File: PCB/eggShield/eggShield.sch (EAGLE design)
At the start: 23 parts, among them U1 V_REG_LDOSMD, U2 V_REG_LDOSMD

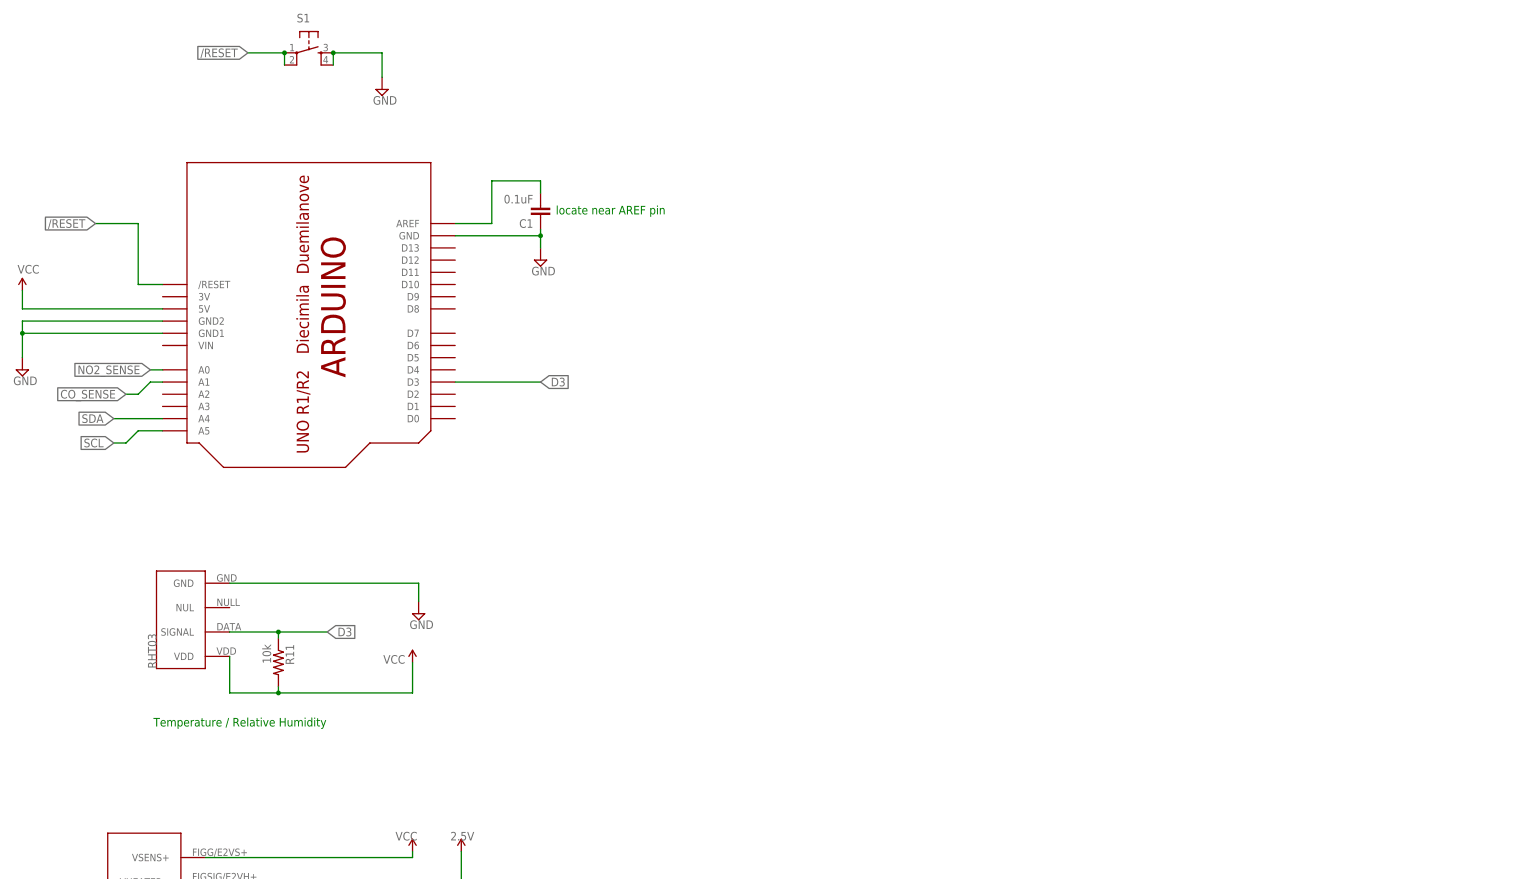
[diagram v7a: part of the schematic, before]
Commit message: added 2:1 I2C Multiplexer
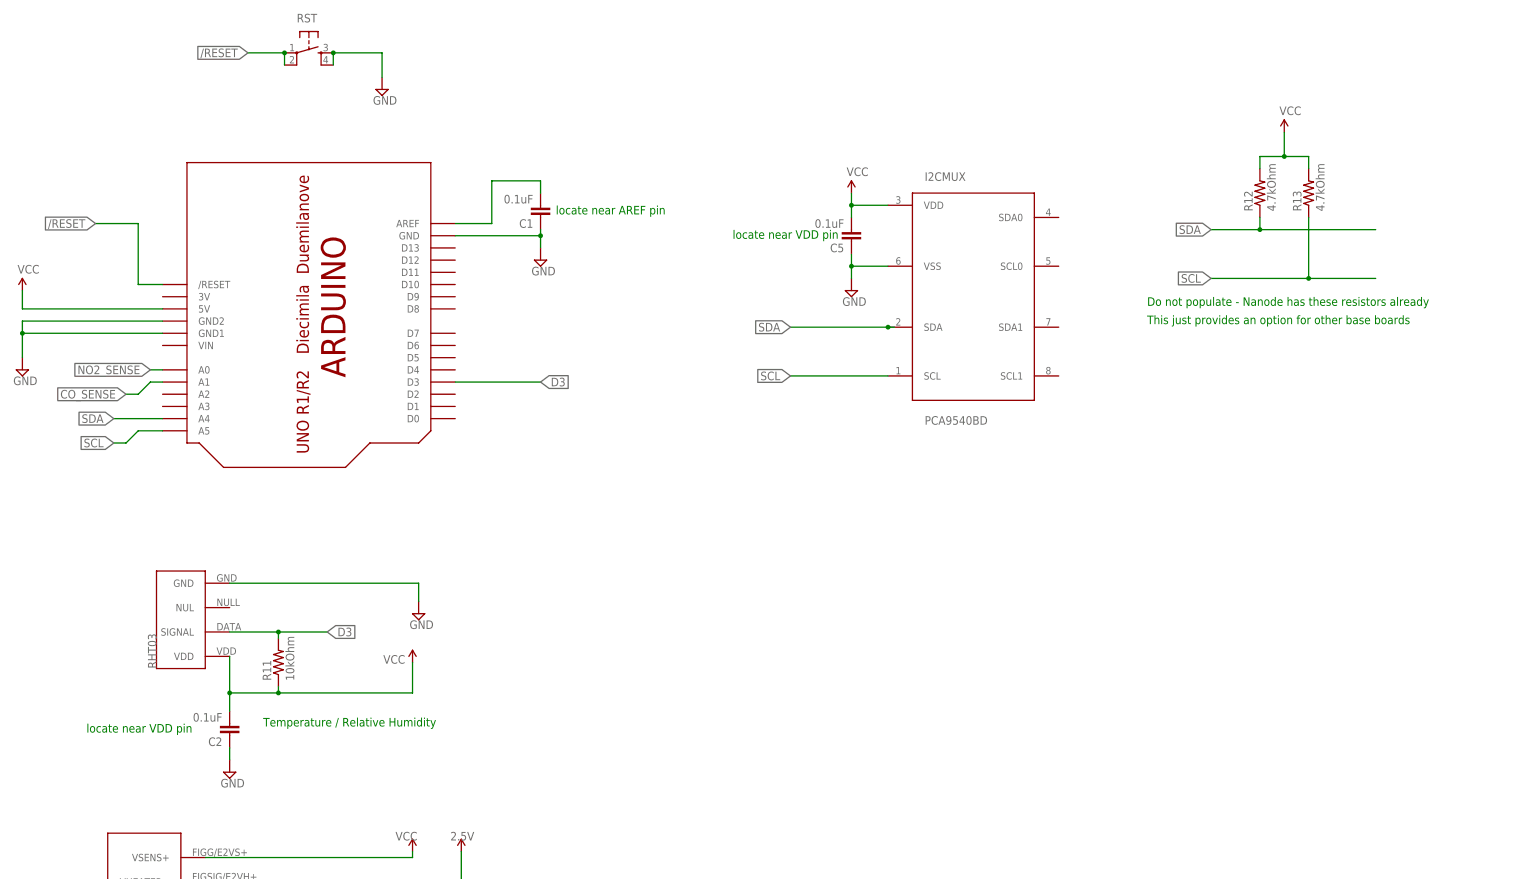
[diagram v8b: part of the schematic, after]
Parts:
- added C2, C5: 0.1uF, SparkFun:CAP0603-CAP
- added I2CMUX: PCA9540BD, wicked-device:PCA9540BD
- added R12, R13: 4.7kOhm, SparkFun:RESISTOR0805-RES
- R11: value 10k -> 10kOhm; device rcl:R-US_R1206 -> SparkFun:RESISTOR0805-RES
- renumbered S1 to RST
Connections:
- net D3: now also R11.2; no longer R11.1
- net GND: now also C2.1, C5.1, I2CMUX.VSS
- net SCL: now also I2CMUX.SCL, R13.1
- net SDA: now also I2CMUX.SDA, R12.1
- net VCC: now also C2.2, C5.2, I2CMUX.VDD, R11.1, R12.2, R13.2; no longer R11.2
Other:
- note added: "Do not populate - Nanode has these resistors already"
- note added: "This just provides an option for other base boards"
- note added: "locate near VDD pin"
- moved on the sheet: R11
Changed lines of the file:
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@@
 <setting verticaltext="up"/>
 </settings>
-<grid distance="0.1" unitdist="inch" unit="inch" style="lines" multiple="1" display="no" altdistance="0.01" altunitdist="inch" altunit="inch"/>
+<grid distance="0.05" unitdist="inch" unit="inch" style="lines" multiple="1" display="no" altdistance="0.01" altunitdist="inch" altunit="inch"/>
 <layers>
 <layer number="1" name="Top" color="4" fill="1" visible="no" active="no"/>
@@
 <part name="R10" library="SparkFun" deviceset="RESISTOR" device="0805-RES"/>
 <part name="DHT22" library="ricardo" deviceset="RHT03" device=""/>
-<part name="R11" library="rcl" deviceset="R-US_" device="R1206" value="10k"/>
 <part name="U$7" library="adafruit" deviceset="ARDUINO" device="-NOHOLE"/>
 <part name="U$8" library="SparkFun" deviceset="1.8V" device="" value="VCC"/>
@@
 <part name="SUPPLY5" library="supply2" deviceset="GND" device=""/>
 <part name="C1" library="SparkFun" deviceset="CAP" device="0603-CAP" value="0.1uF"/>
-<part name="S1" library="SparkFun" deviceset="TAC_SWITCH" device="SMD"/>
+<part name="RST" library="SparkFun" deviceset="TAC_SWITCH" device="SMD"/>
 <part name="SUPPLY7" library="supply2" deviceset="GND" device=""/>
+<part name="C2" library="SparkFun" deviceset="CAP" device="0603-CAP" value="0.1uF"/>
+<part name="SUPPLY8" library="supply2" deviceset="GND" device=""/>
+<part name="I2CMUX" library="wicked-device" deviceset="PCA9540B" device="D"/>
+<part name="C5" library="SparkFun" deviceset="CAP" device="0603-CAP" value="0.1uF"/>
+<part name="SUPPLY10" library="supply2" deviceset="GND" device=""/>
+<part name="P+2" library="SparkFun" deviceset="VCC" device=""/>
+<part name="R11" library="SparkFun" deviceset="RESISTOR" device="0805-RES" value="10kOhm"/>
+<part name="R12" library="SparkFun" deviceset="RESISTOR" device="0805-RES" value="4.7kOhm"/>
+<part name="R13" library="SparkFun" deviceset="RESISTOR" device="0805-RES" value="4.7kOhm"/>
+<part name="P+4" library="SparkFun" deviceset="VCC" device=""/>
 </parts>
 <sheets>
@@
 <text x="90.805" y="126.365" size="1.778" layer="91">locate near OUT pin</text>
 <text x="137.795" y="65.405" size="1.778" layer="91">CO Sensor</text>
-<text x="145.415" y="118.745" size="1.778" layer="91">Temperature / Relative Humidity</text>
+<text x="168.275" y="118.745" size="1.778" layer="91">Temperature / Relative Humidity</text>
 <text x="229.235" y="225.425" size="1.778" layer="91">locate near AREF pin</text>
+<text x="131.445" y="117.475" size="1.778" layer="91">locate near VDD pin</text>
+<text x="266.065" y="220.345" size="1.778" layer="91">locate near VDD pin</text>
+<text x="352.425" y="206.375" size="1.778" layer="91">Do not populate - Nanode has these resistors already</text>
+<text x="352.425" y="202.565" size="1.778" layer="91">This just provides an option for other base boards</text>
 </plain>
 <instances>
@@
 <instance part="R10" gate="G$1" x="177.8" y="39.37" rot="R90"/>
 <instance part="DHT22" gate="G$1" x="161.29" y="148.59" rot="R90"/>
-<instance part="R11" gate="G$1" x="171.45" y="132.08" rot="R270"/>
 <instance part="U$7" gate="G$1" x="180.34" y="213.36" rot="R270"/>
 <instance part="U$8" gate="G$1" x="199.39" y="132.08" smashed="yes">
@@
 <instance part="SUPPLY5" gate="GND" x="226.06" y="215.9"/>
 <instance part="C1" gate="G$1" x="226.06" y="227.33" rot="R180"/>
-<instance part="S1" gate="S" x="177.8" y="259.08"/>
+<instance part="RST" gate="S" x="177.8" y="259.08"/>
 <instance part="SUPPLY7" gate="GND" x="193.04" y="251.46"/>
+<instance part="C2" gate="G$1" x="161.29" y="119.38" rot="R180"/>
+<instance part="SUPPLY8" gate="GND" x="161.29" y="109.22"/>
+<instance part="I2CMUX" gate="G$1" x="316.23" y="209.55"/>
+<instance part="C5" gate="G$1" x="290.83" y="222.25" rot="R180"/>
+<instance part="SUPPLY10" gate="GND" x="290.83" y="209.55"/>
+<instance part="P+2" gate="1" x="290.83" y="229.87"/>
+<instance part="R11" gate="G$1" x="171.45" y="132.08" rot="R90"/>
+<instance part="R12" gate="G$1" x="375.92" y="229.87" rot="R90"/>
+<instance part="R13" gate="G$1" x="386.08" y="229.87" rot="R90"/>
+<instance part="P+4" gate="1" x="381" y="242.57"/>
 </instances>
 <busses>
@@
 </segment>
 <segment>
-<pinref part="DHT22" gate="G$1" pin="VDD"/>
 <wire x1="199.39" y1="125.73" x2="171.45" y2="125.73" width="0.1524" layer="91"/>
-<wire x1="171.45" y1="125.73" x2="161.29" y2="125.73" width="0.1524" layer="91"/>
-<wire x1="161.29" y1="125.73" x2="161.29" y2="133.35" width="0.1524" layer="91"/>
-<pinref part="R11" gate="G$1" pin="2"/>
 <wire x1="171.45" y1="127" x2="171.45" y2="125.73" width="0.1524" layer="91"/>
 <junction x="171.45" y="125.73"/>
 <pinref part="U$8" gate="G$1" pin="1.8V"/>
 <wire x1="199.39" y1="125.73" x2="199.39" y2="132.08" width="0.1524" layer="91"/>
+<pinref part="R11" gate="G$1" pin="1"/>
+<pinref part="DHT22" gate="G$1" pin="VDD"/>
+<wire x1="161.29" y1="121.92" x2="161.29" y2="125.73" width="0.1524" layer="91"/>
+<pinref part="C2" gate="G$1" pin="2"/>
+<wire x1="161.29" y1="125.73" x2="161.29" y2="133.35" width="0.1524" layer="91"/>
+<wire x1="171.45" y1="125.73" x2="161.29" y2="125.73" width="0.1524" layer="91"/>
+<junction x="161.29" y="125.73"/>
 </segment>
 <segment>
@@
 <wire x1="147.32" y1="205.74" x2="118.11" y2="205.74" width="0.1524" layer="91"/>
 <wire x1="118.11" y1="205.74" x2="118.11" y2="209.55" width="0.1524" layer="91"/>
+</segment>
+<segment>
+<pinref part="I2CMUX" gate="G$1" pin="VDD"/>
+<pinref part="C5" gate="G$1" pin="2"/>
+<wire x1="298.45" y1="227.33" x2="290.83" y2="227.33" width="0.1524" layer="91"/>
+<wire x1="290.83" y1="227.33" x2="290.83" y2="224.79" width="0.1524" layer="91"/>
+<wire x1="290.83" y1="227.33" x2="290.83" y2="229.87" width="0.1524" layer="91"/>
+<junction x="290.83" y="227.33"/>
+<pinref part="P+2" gate="1" pin="VCC"/>
+</segment>
+<segment>
+<pinref part="R12" gate="G$1" pin="2"/>
+<wire x1="375.92" y1="234.95" x2="375.92" y2="237.49" width="0.1524" layer="91"/>
+<pinref part="R13" gate="G$1" pin="2"/>
+<wire x1="375.92" y1="237.49" x2="381" y2="237.49" width="0.1524" layer="91"/>
+<wire x1="381" y1="237.49" x2="386.08" y2="237.49" width="0.1524" layer="91"/>
+<wire x1="386.08" y1="237.49" x2="386.08" y2="234.95" width="0.1524" layer="91"/>
+<wire x1="381" y1="237.49" x2="381" y2="242.57" width="0.1524" layer="91"/>
+<junction x="381" y="237.49"/>
+<pinref part="P+4" gate="1" pin="VCC"/>
 </segment>
 </net>
@@
 </segment>
 <segment>
-<pinref part="S1" gate="S" pin="3"/>
-<pinref part="S1" gate="S" pin="4"/>
+<pinref part="RST" gate="S" pin="3"/>
+<pinref part="RST" gate="S" pin="4"/>
 <wire x1="182.88" y1="259.08" x2="182.88" y2="256.54" width="0.1524" layer="91"/>
 <junction x="182.88" y="259.08"/>
@@
 <pinref part="SUPPLY7" gate="GND" pin="GND"/>
 <wire x1="193.04" y1="259.08" x2="193.04" y2="254" width="0.1524" layer="91"/>
+</segment>
+<segment>
+<pinref part="C2" gate="G$1" pin="1"/>
+<wire x1="161.29" y1="114.3" x2="161.29" y2="111.76" width="0.1524" layer="91"/>
+<pinref part="SUPPLY8" gate="GND" pin="GND"/>
+</segment>
+<segment>
+<pinref part="I2CMUX" gate="G$1" pin="VSS"/>
+<pinref part="C5" gate="G$1" pin="1"/>
+<wire x1="298.45" y1="214.63" x2="290.83" y2="214.63" width="0.1524" layer="91"/>
+<wire x1="290.83" y1="214.63" x2="290.83" y2="217.17" width="0.1524" layer="91"/>
+<wire x1="290.83" y1="214.63" x2="290.83" y2="212.09" width="0.1524" layer="91"/>
+<junction x="290.83" y="214.63"/>
+<pinref part="SUPPLY10" gate="GND" pin="GND"/>
 </segment>
 </net>
@@
 <wire x1="161.29" y1="138.43" x2="171.45" y2="138.43" width="0.1524" layer="91"/>
 <wire x1="171.45" y1="138.43" x2="181.61" y2="138.43" width="0.1524" layer="91"/>
-<pinref part="R11" gate="G$1" pin="1"/>
 <label x="181.61" y="138.43" size="1.778" layer="95" xref="yes"/>
 <wire x1="171.45" y1="138.43" x2="171.45" y2="137.16" width="0.1524" layer="91"/>
 <junction x="171.45" y="138.43"/>
+<pinref part="R11" gate="G$1" pin="2"/>
 </segment>
 <segment>
@@
 </segment>
 <segment>
-<pinref part="S1" gate="S" pin="1"/>
-<pinref part="S1" gate="S" pin="2"/>
+<pinref part="RST" gate="S" pin="1"/>
+<pinref part="RST" gate="S" pin="2"/>
 <wire x1="172.72" y1="259.08" x2="172.72" y2="256.54" width="0.1524" layer="91"/>
 <junction x="172.72" y="259.08"/>
@@
 <label x="137.16" y="182.88" size="1.778" layer="95" rot="R180" xref="yes"/>
 </segment>
+<segment>
+<wire x1="299.72" y1="201.93" x2="298.45" y2="201.93" width="0.1524" layer="91"/>
+<label x="278.13" y="201.93" size="1.778" layer="95" rot="R180" xref="yes"/>
+<pinref part="I2CMUX" gate="G$1" pin="SDA"/>
+<wire x1="298.45" y1="201.93" x2="278.13" y2="201.93" width="0.1524" layer="91"/>
+<junction x="298.45" y="201.93"/>
+</segment>
+<segment>
+<label x="365.76" y="222.25" size="1.778" layer="95" rot="R180" xref="yes"/>
+<wire x1="400.05" y1="222.25" x2="375.92" y2="222.25" width="0.1524" layer="91"/>
+<pinref part="R12" gate="G$1" pin="1"/>
+<wire x1="375.92" y1="222.25" x2="365.76" y2="222.25" width="0.1524" layer="91"/>
+<wire x1="375.92" y1="224.79" x2="375.92" y2="222.25" width="0.1524" layer="91"/>
+<junction x="375.92" y="222.25"/>
+</segment>
 </net>
 <net name="SCL" class="0">
@@
 <label x="137.16" y="177.8" size="1.778" layer="95" rot="R180" xref="yes"/>
 </segment>
-</net>
+<segment>
+<pinref part="I2CMUX" gate="G$1" pin="SCL"/>
+<wire x1="298.45" y1="191.77" x2="278.13" y2="191.77" width="0.1524" layer="91"/>
+<label x="278.13" y="191.77" size="1.778" layer="95" rot="R180" xref="yes"/>
+</segment>
+<segment>
+<wire x1="400.05" y1="212.09" x2="386.08" y2="212.09" width="0.1524" layer="91"/>
+<label x="365.76" y="212.09" size="1.778" layer="95" rot="R180" xref="yes"/>
+<pinref part="R13" gate="G$1" pin="1"/>
+<wire x1="386.08" y1="212.09" x2="365.76" y2="212.09" width="0.1524" layer="91"/>
+<wire x1="386.08" y1="224.79" x2="386.08" y2="212.09" width="0.1524" layer="91"/>
+<junction x="386.08" y="212.09"/>
+</segment>
+</net>
